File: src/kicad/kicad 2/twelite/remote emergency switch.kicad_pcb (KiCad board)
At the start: 2 copper layers, 47.9 x 49.5 mm, 27 parts

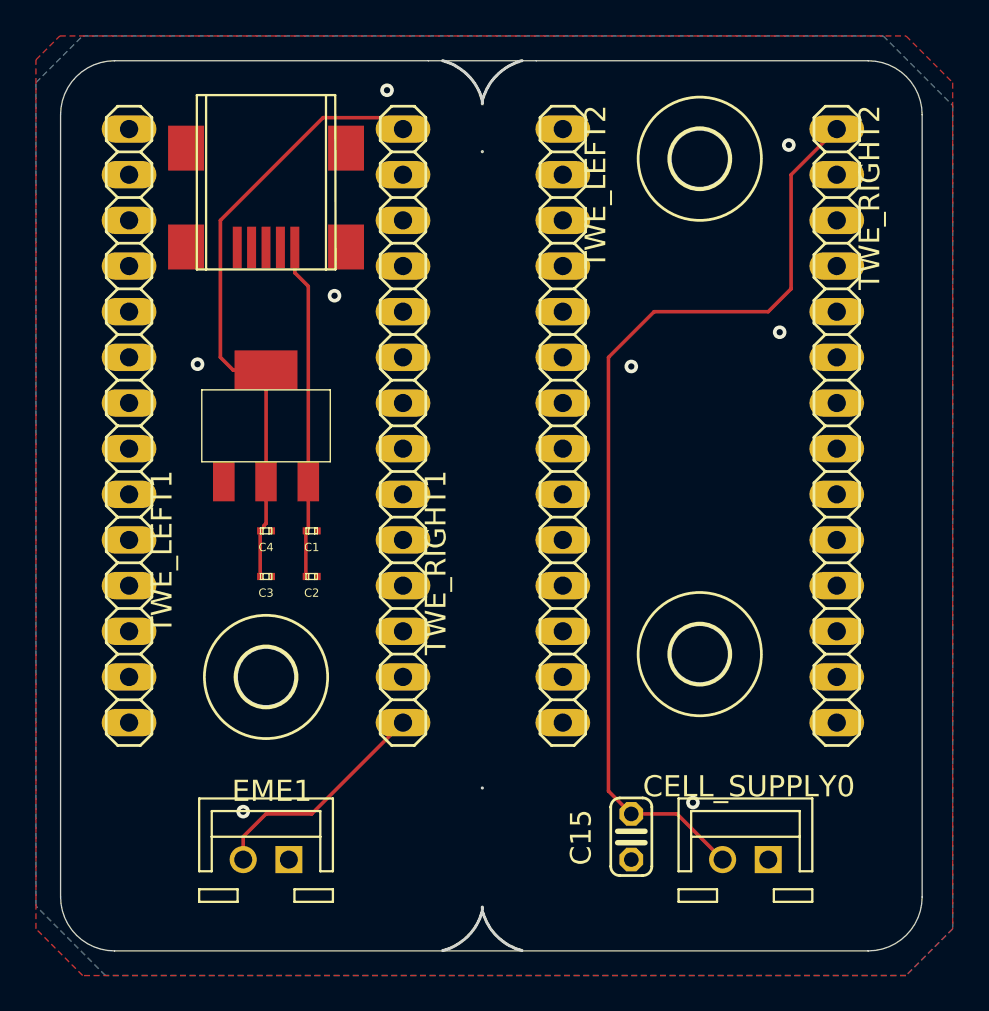
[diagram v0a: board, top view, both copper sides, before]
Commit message: fix twelite circuit slot
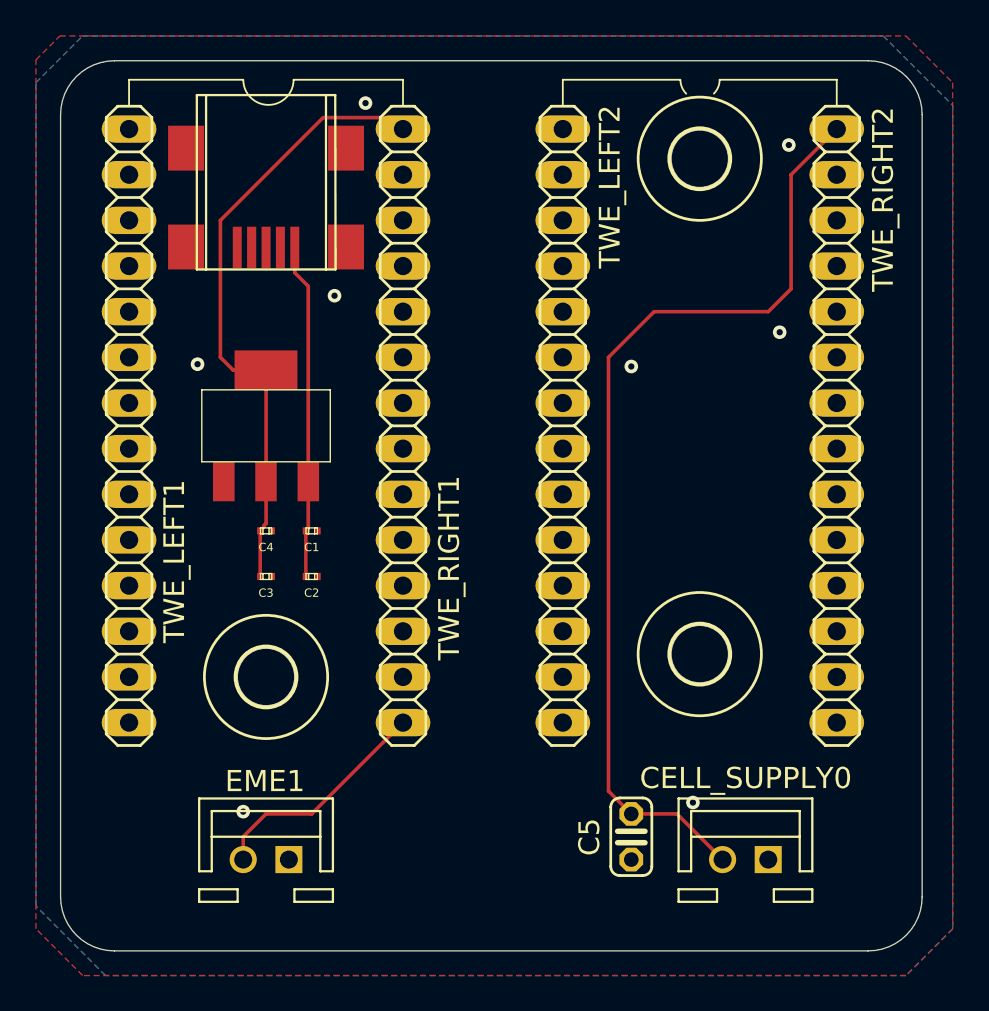
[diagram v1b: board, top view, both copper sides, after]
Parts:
- removed the ? at (148.0, 120.7)
- removed the ? at (148.0, 127.3)
- removed the ? at (148.0, 82.5)
- removed the ? at (148.0, 85.3)
- removed the ? at (148.0, 82.6)
- removed the ? at (148.0, 82.7)
- removed the ? at (148.0, 83.8)
- removed REF**: corner-holedown, remote emergency switch:corner-holedown
- removed REF**: corner-hole, remote emergency switch:corner-hole
- added ?: , , F.Cu at (147.9, 83.7)
- moved ? 33.9 mm to (181.7, 101.3)
- moved ? 2.14 mm to (148.1, 126.2)
- renumbered C15 to C5
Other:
- outline, holes or cut-outs redrawn
